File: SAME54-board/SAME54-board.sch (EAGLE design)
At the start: 25 parts, among them IC1 ATSAME54N20A-AUT, J1 GSD09002SEU

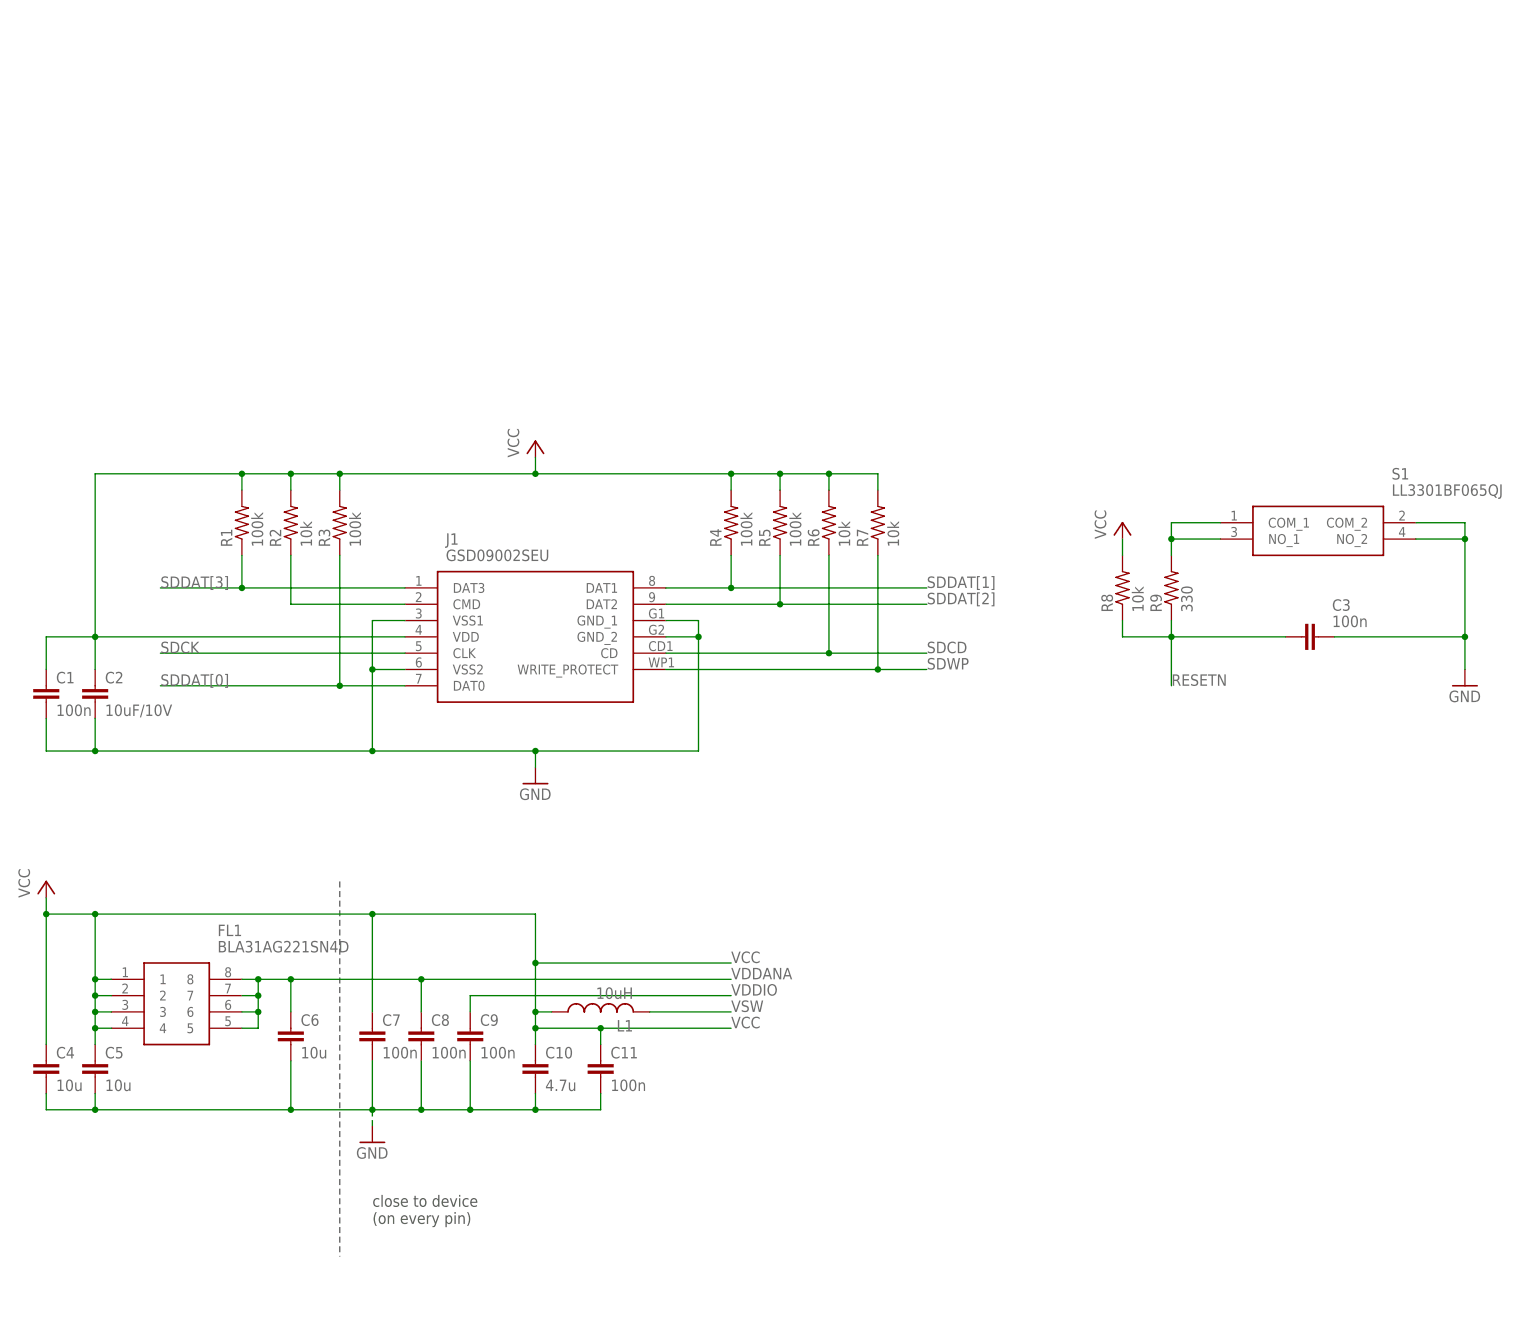
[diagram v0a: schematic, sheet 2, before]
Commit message: Designed board for all pre-determined peripherals needed.
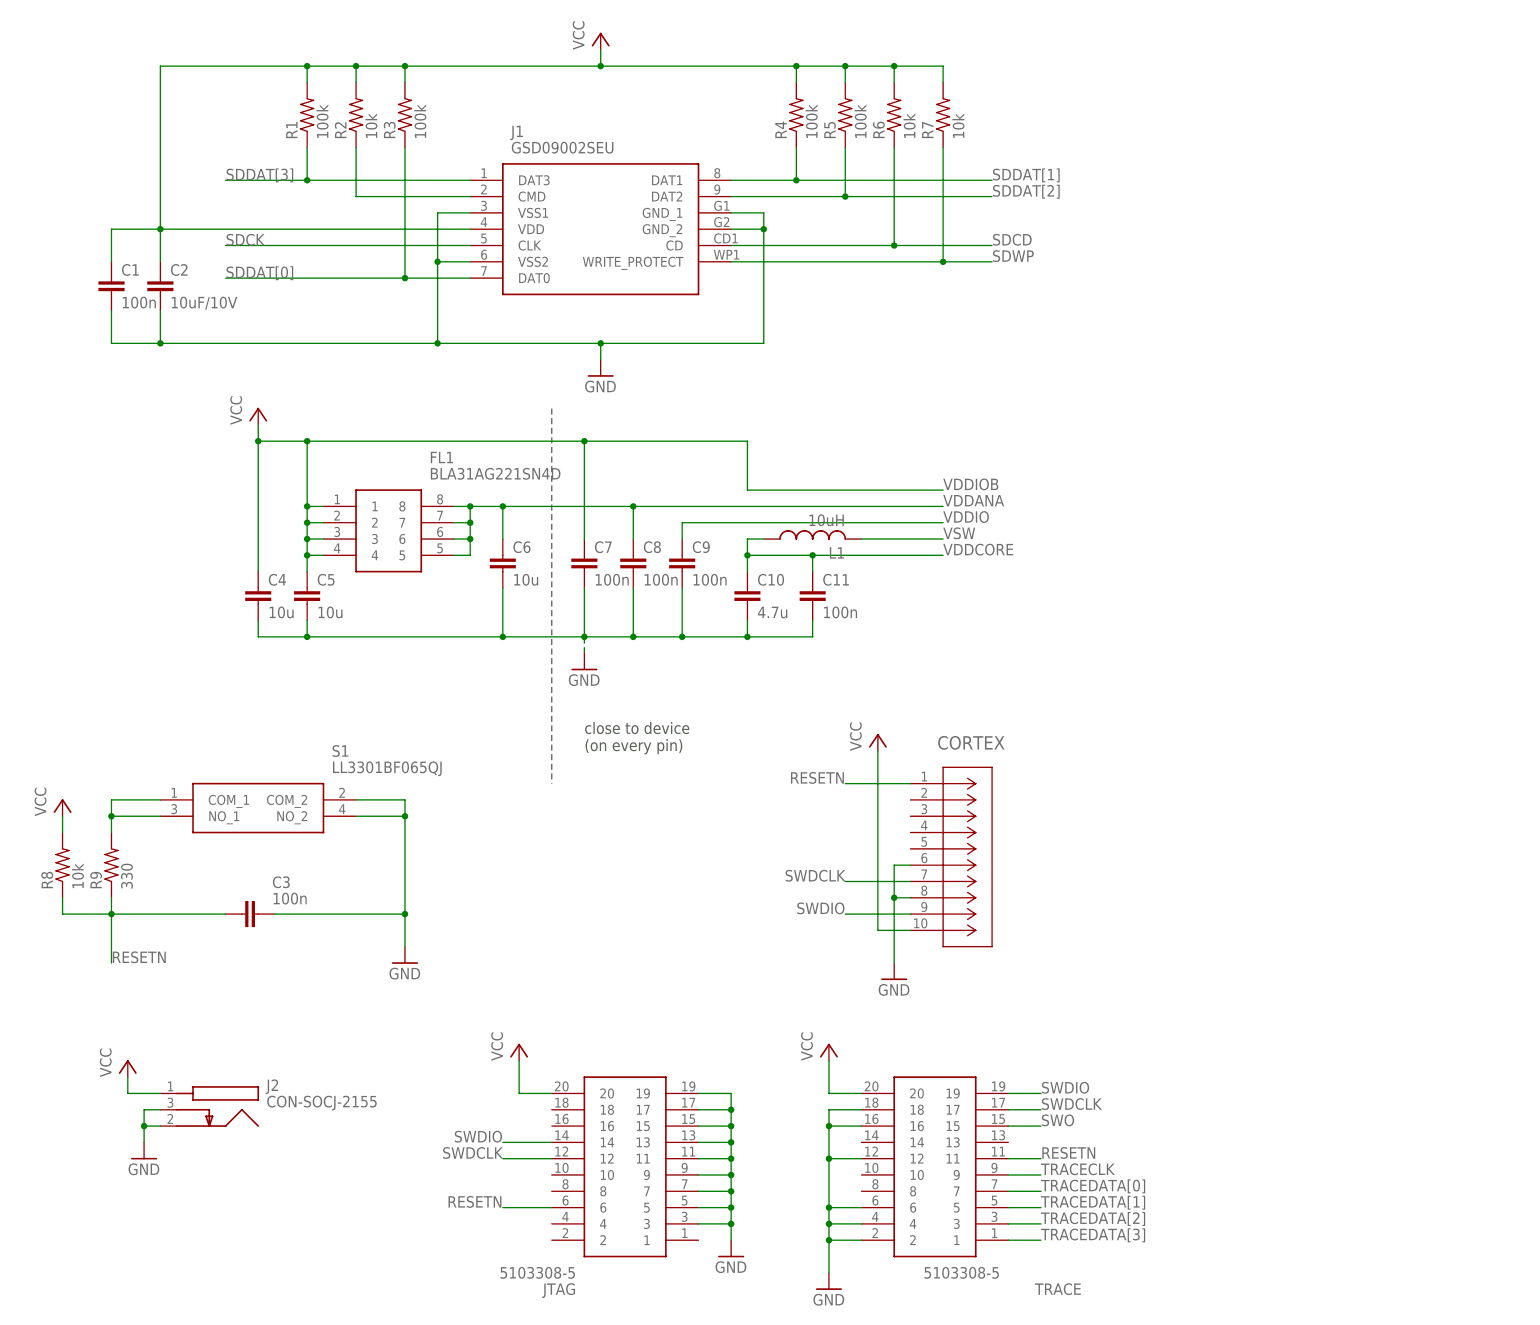
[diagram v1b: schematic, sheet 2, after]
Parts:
- added CORTEX: 5103308-1, SamacSys_Parts:5103308-1
- added J2: CON-SOCJ-2155, SamacSys_Parts:CON-SOCJ-2155
- added JP1, JP2: (no value), pinhead:PINHD-1X25
- added JP7: (no value), pinhead:PINHD-1X17
- added JTAG, TRACE: 5103308-5, SamacSys_Parts:5103308-5
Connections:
- new net N$1: IC1.PC07, JP2.5
- new net N$10: IC1.PA04, JP2.11
- new net N$11: IC1.PB09, JP2.12
- new net N$12: IC1.PB08, JP2.13
- new net N$13: IC1.PB07, JP2.14
- new net N$14: IC1.PB06, JP2.15
- new net N$15: IC1.PB05, JP2.16
- new net N$16: IC1.PB04, JP2.17
- new net N$17: IC1.PA03, JP2.18
- new net N$18: IC1.PA02, JP2.19
- new net N$19: IC1.PC03, JP2.20
- new net N$20: IC1.PC02, JP2.21
- new net N$21: IC1.PC01, JP2.22
- new net N$22: IC1.PC00, JP2.23
- new net N$23: IC1.PA01, JP2.24
- new net N$24: IC1.PA21, JP7.17
- new net N$25: IC1.PA22, JP7.16
- new net N$26: IC1.PA23, JP7.15
- new net N$27: IC1.PA24, JP7.14
- new net N$28: IC1.PA25, JP7.13
- new net N$29: IC1.PA20, JP1.1
- new net N$3: IC1.PC06, JP2.6
- new net N$30: IC1.PB21, JP1.2
- new net N$31: IC1.PB20, JP1.3
- new net N$32: IC1.PB19, JP1.4
- new net N$33: IC1.PB18, JP1.5
- new net N$34: IC1.PB17, JP1.6
- new net N$35: IC1.PB16, JP1.7
- new net N$36: IC1.PC21, JP1.8
- new net N$37: IC1.PC20, JP1.9
- new net N$38: IC1.PC19, JP1.10
- new net N$39: IC1.PC18, JP1.11
- new net N$40: IC1.PC17, JP1.12
- new net N$41: IC1.PC16, JP1.13
- new net N$42: IC1.PA19, JP1.14
- new net N$43: IC1.PA18, JP1.15
- new net N$44: IC1.PA17, JP1.16
- new net N$45: IC1.PA16, JP1.17
- new net N$46: IC1.PA15, JP1.18
- new net N$47: IC1.PA14, JP1.19
- new net N$48: IC1.PC11, JP2.1
- new net N$49: IC1.PA13, JP1.20
- new net N$5: IC1.PC05, JP2.7
- new net N$50: IC1.PA12, JP1.21
- new net N$51: IC1.PC15, JP1.22
- new net N$52: IC1.PC14, JP1.23
- new net N$53: IC1.PC13, JP1.24
- new net N$54: IC1.PC12, JP1.25
- new net N$55: IC1.PC10, JP2.2
- new net N$56: IC1.PB15, JP2.3
- new net N$57: IC1.PB14, JP2.4
- new net N$58: IC1.PA00, JP2.25
- new net N$59: IC1.PB31, JP7.7
- new net N$6: IC1.PA07, JP2.8
- new net N$60: IC1.PB00, JP7.6
- new net N$61: IC1.PB01, JP7.5
- new net N$62: IC1.PB03, JP7.3
- new net N$63: IC1.PB02, JP7.4
- new net N$64: IC1.PB22, JP7.12
- new net N$65: IC1.PB23, JP7.11
- new net N$66: IC1.PB24, JP7.10
- new net N$67: IC1.PB25, JP7.9
- new net N$68: IC1.PA27, JP7.8
- new net N$8: IC1.PA06, JP2.9
- new net N$9: IC1.PA05, JP2.10
- new net SWDCLK: CORTEX.7, IC1.PA30, JTAG.12, TRACE.17
- new net SWDIO: CORTEX.9, IC1.PA31, JTAG.14, TRACE.19
- new net SWO: IC1.PB30, TRACE.15
- new net TRACECLK: IC1.PC27, TRACE.9
- new net TRACEDATA[0]: IC1.PC28, TRACE.7
- new net TRACEDATA[1]: IC1.PC26, TRACE.5
- new net TRACEDATA[2]: IC1.PC25, TRACE.3
- new net TRACEDATA[3]: IC1.PC24, TRACE.1
- new net VDDCORE: C10.1, C11.1, IC1.VDDCORE, L1.1
- net GND: now also CORTEX.6, CORTEX.8, J2.2, J2.3, JP7.2, JTAG.11, JTAG.13, JTAG.15, JTAG.17, JTAG.19, JTAG.3, JTAG.5, JTAG.7, JTAG.9, TRACE.12, TRACE.16, TRACE.18, TRACE.2, TRACE.4, TRACE.6
- net RESETN: now also CORTEX.1, JTAG.6, TRACE.11
- net VCC: now also CORTEX.10, J2.1, JP7.1, JTAG.20, TRACE.20; no longer C10.1, C11.1, C4.1, C5.1, C7.1, FL1.1, FL1.2, FL1.3, FL1.4, IC1.VDDCORE, L1.1
- net VDDIOB: now also C4.1, C5.1, C7.1, FL1.1, FL1.2, FL1.3, FL1.4
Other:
- moved on the sheet: C1, C10, C11, C2, C3, C4, C5, C6, C7, C8, C9, FL1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

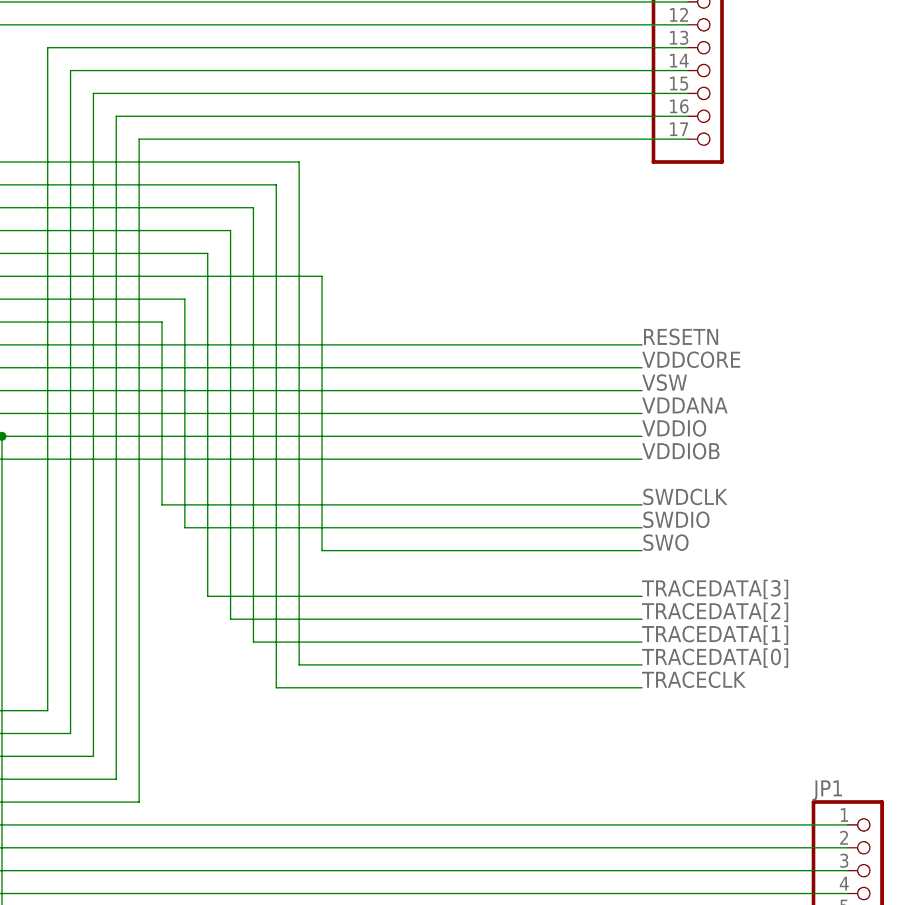
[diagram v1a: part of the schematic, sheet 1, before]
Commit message: Added drill holes and correct power supply mistake
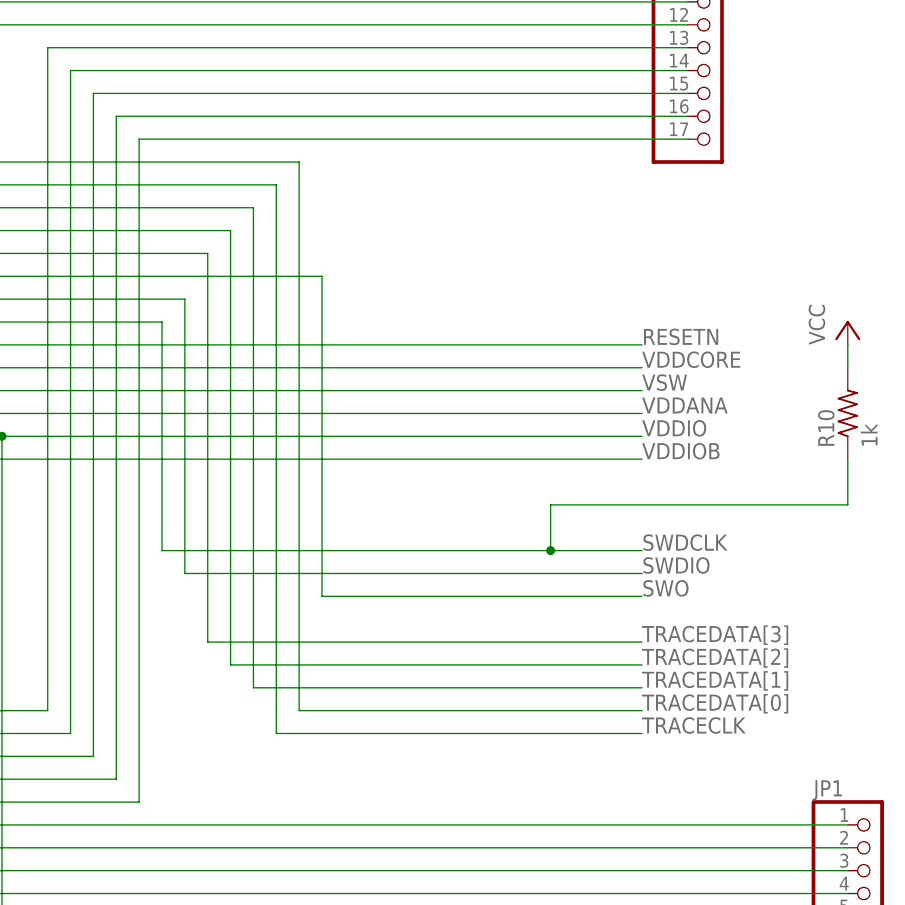
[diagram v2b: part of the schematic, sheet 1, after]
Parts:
- added R10: 1k, rcl:R-US_M1206
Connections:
- net SWDCLK: now also R10.1
- net VCC: now also R10.2
- net VDDIO: now also C5.1, FL1.1, FL1.2, FL1.3, FL1.4
- net VDDIOB: no longer C5.1, FL1.1, FL1.2, FL1.3, FL1.4
